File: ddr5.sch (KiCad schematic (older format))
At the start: 42 parts, among them U1 MT60B2G8HB-48B_A

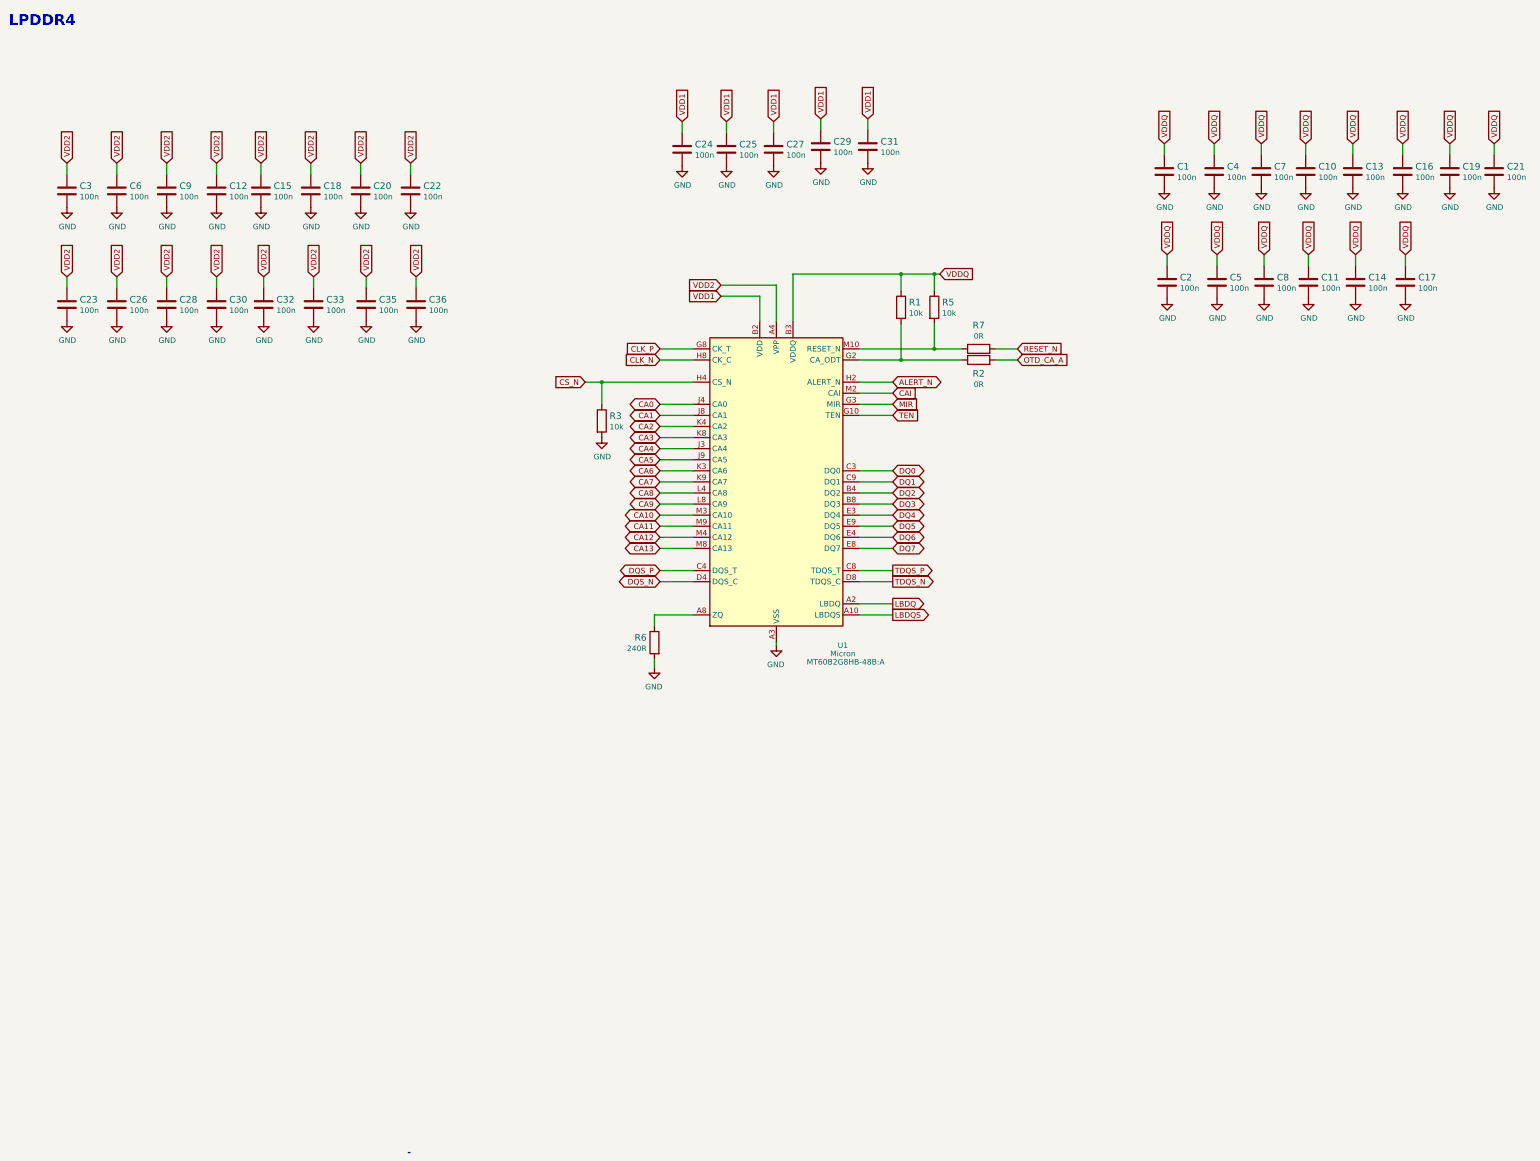
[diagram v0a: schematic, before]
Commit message: Reduce number of capacitors to match supply pin count, add OR resistors for control signals
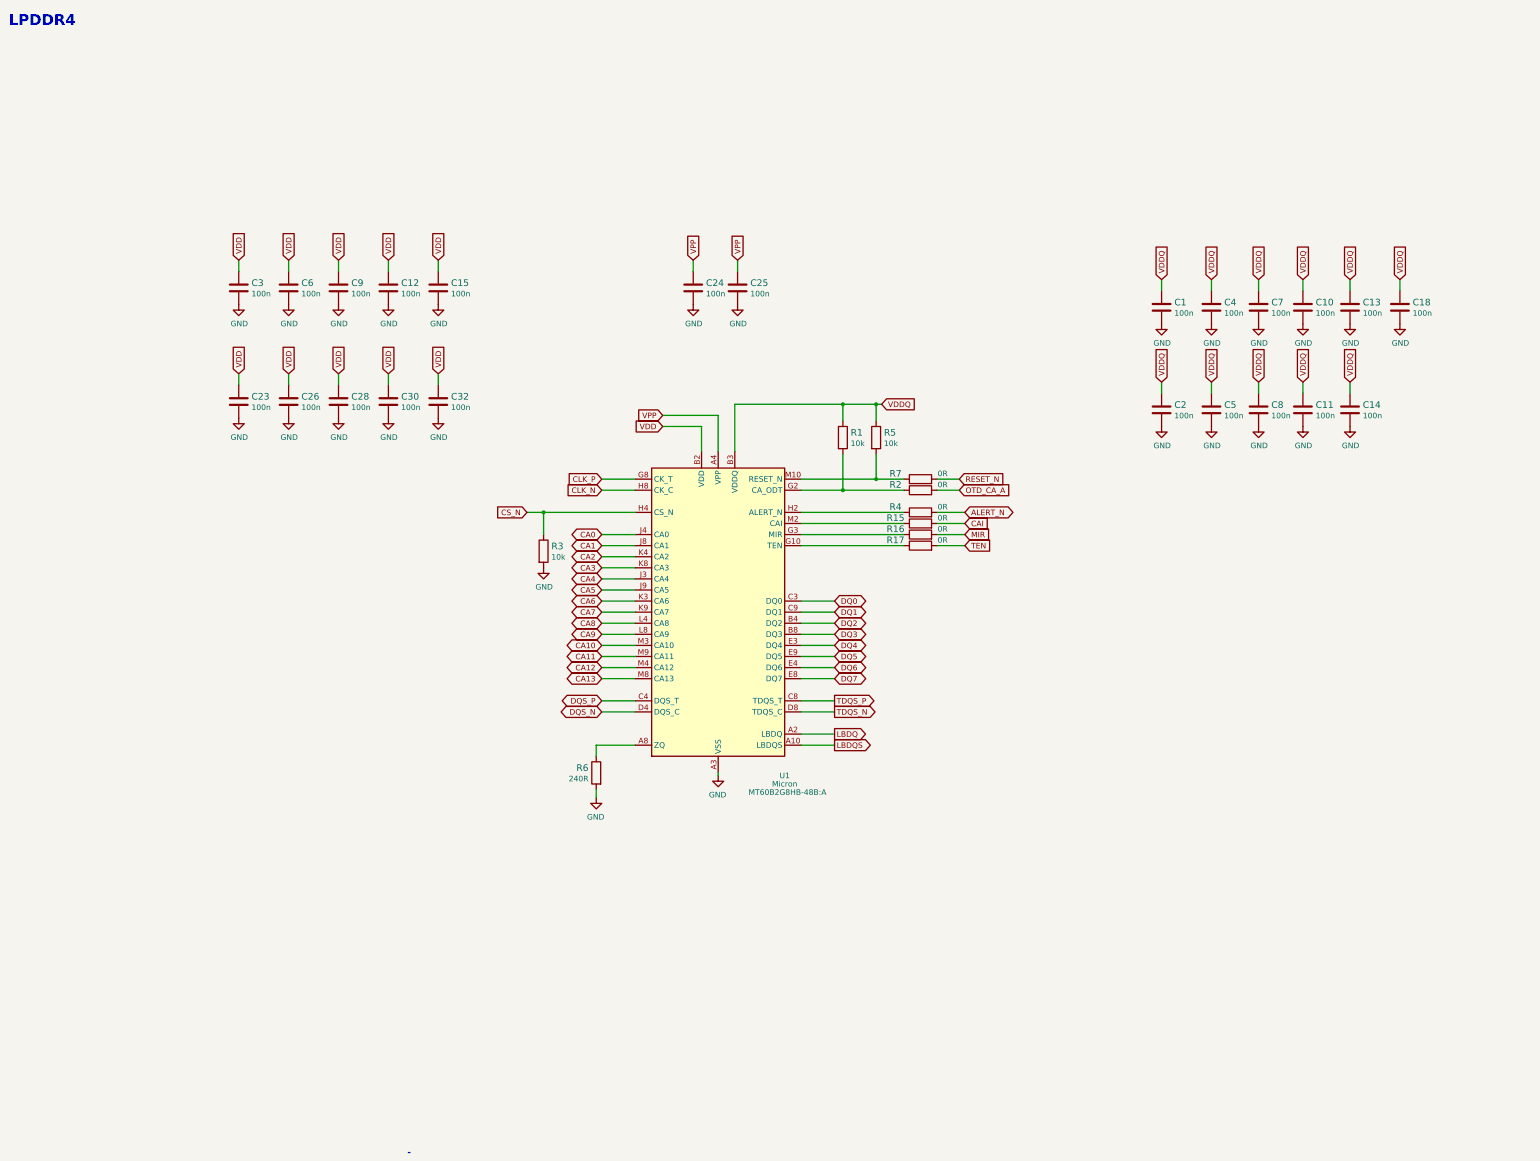
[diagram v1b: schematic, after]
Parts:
- removed C16, C17, C19, C20, C21, C22, C27, C29, C31, C33, C35, C36: C_100n_0201, ddr5-testbed-footprints:0201-res, symbol ddr5-testbed:C_100n_0201
- added R15, R16, R17, R4: R_0R_0402, ddr5-testbed-footprints:0402-res, symbol ddr5-testbed:R_0R_0402
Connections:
- net ALERT_N: now also R4.2; no longer U1.H2 (ALERT_N)
- net CAI: now also R15.2; no longer U1.M2 (CAI)
- net MIR: now also R16.2; no longer U1.G3 (MIR)
- net TEN: now also R17.2; no longer U1.G10 (TEN)
- net VDD: now also C12.1, C15.1, C23.1, C26.1, C28.1, C3.1, C30.1, C32.1, C6.1, C9.1; no longer C24.1, C25.1
- net VDDQ: now also C18.1
- net VPP: now also C24.1, C25.1; no longer C12.1, C15.1, C18.1, C23.1, C26.1, C28.1, C3.1, C30.1, C32.1, C6.1, C9.1
- new net: R17.1, U1.G10 (TEN)
- new net: R16.1, U1.G3 (MIR)
- new net: R4.1, U1.H2 (ALERT_N)
- new net: R15.1, U1.M2 (CAI)
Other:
- moved on the sheet: C1, C10, C11, C12, C13, C14, C15, C18, C2, C23, C24, C25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

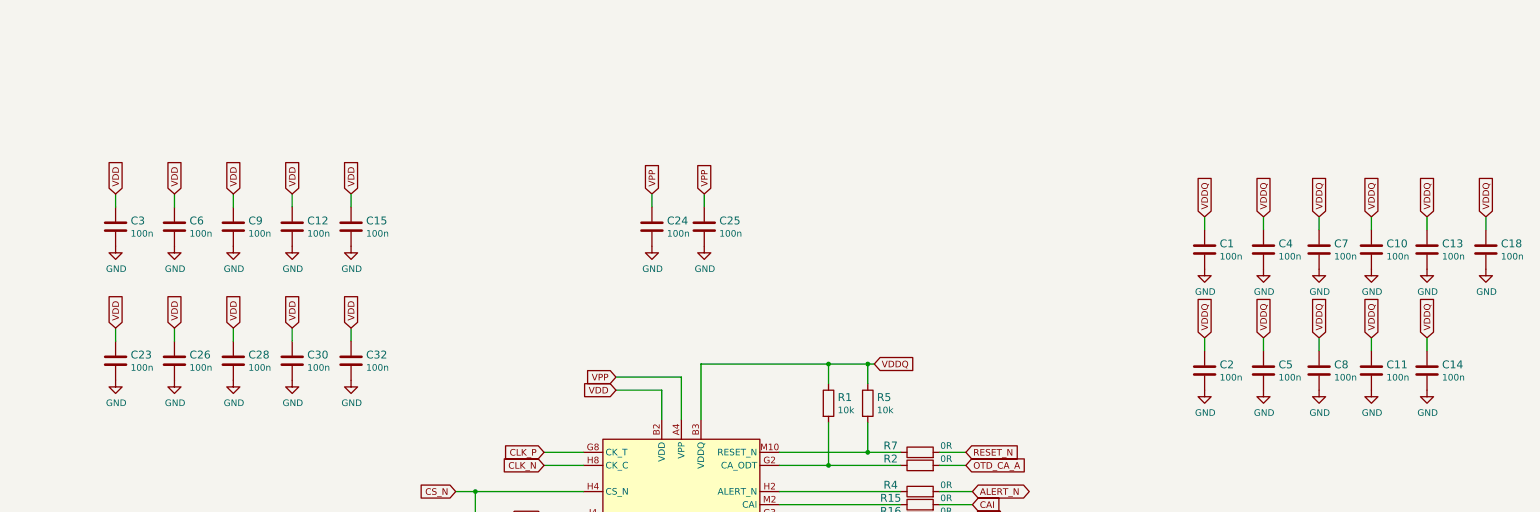
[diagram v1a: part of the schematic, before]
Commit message: Fix power labels naming scheme, remove connection from SODIM to VDDQ, add chockes to DDR5 power
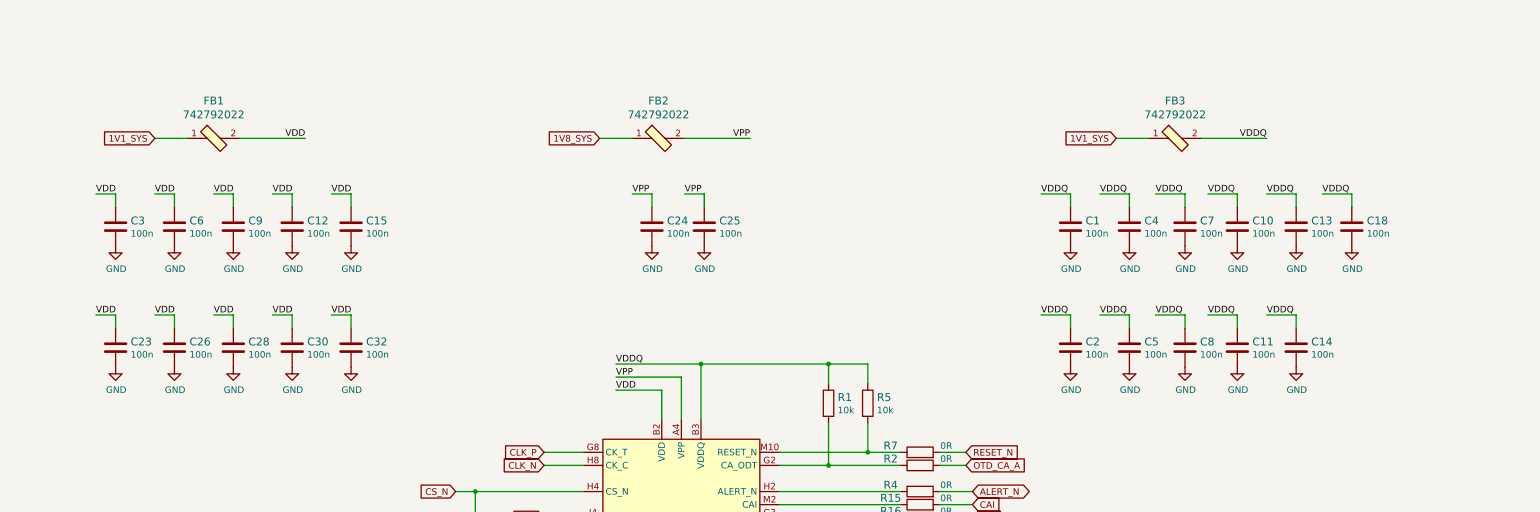
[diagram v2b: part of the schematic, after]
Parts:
- added FB1, FB2, FB3: 742792022, ddr5-testbed-footprints:0805-res, symbol ddr5-testbed:742792022
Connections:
- net VDD: now also FB1.2
- net VDDQ: now also FB3.2
- net VPP: now also FB2.2
- new net 1V1_SYS: FB1.1, FB3.1
- new net 1V8_SYS: FB2.1
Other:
- moved on the sheet: C1, C10, C11, C13, C14, C18, C2, C23, C26, C28, C30, C32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
